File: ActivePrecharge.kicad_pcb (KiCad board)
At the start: 2 copper layers, 71.5 x 54.5 mm, 34 parts, among them Con1 LED, J1 Conn_01x03, J2 Conn_01x02, J3 Conn_01x02, Q1 IRLML0030, U1 NCP785AH50T1G, U2 NCP785AH50T1G, U3 TLV9301xDCK, U4 TCMT1106

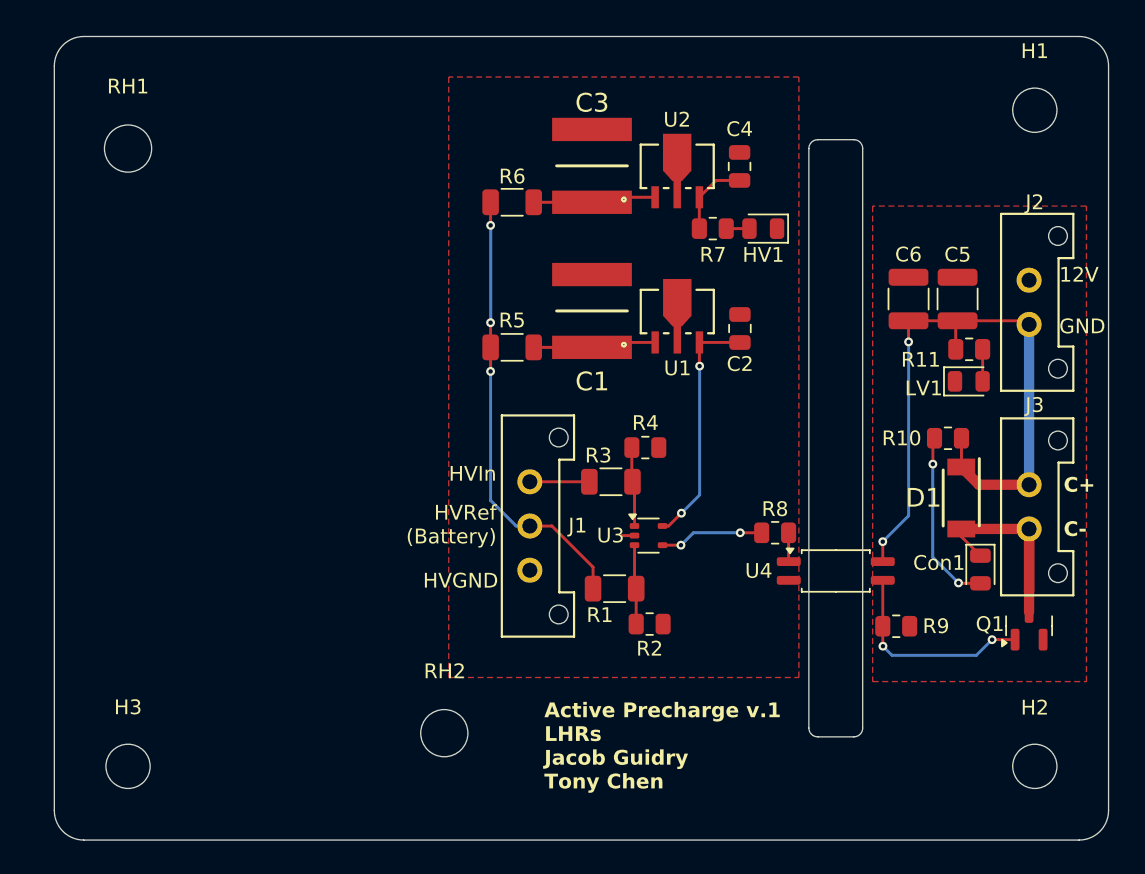
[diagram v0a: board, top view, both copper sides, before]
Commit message: 11/2 fixed incorrect footprint and symbol
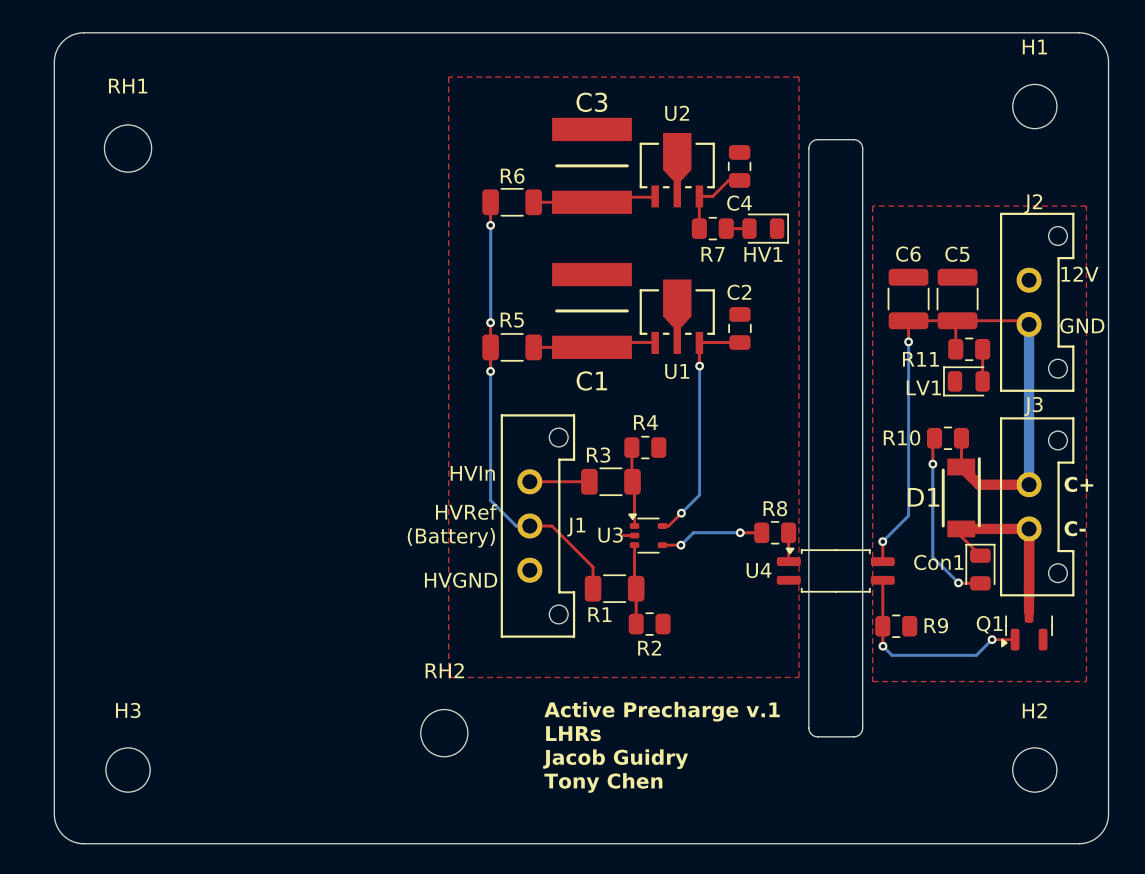
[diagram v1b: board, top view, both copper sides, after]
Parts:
- moved H1 0.25 mm to (140.8, 73.0)
- moved H2 0.25 mm to (140.8, 118.0)
- moved H3 0.25 mm to (79.2, 118.0)
- moved U2 0.06 mm to (116.5, 77.0)
- turned C2 to -90 degrees
- turned C4 to -90 degrees
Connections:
- C2 pad 1: /Vcc+ -> HVGND
- C2 pad 2: HVGND -> /Vcc+
- C4 pad 1: Net-(U2-OUT) -> HVGND
- C4 pad 2: HVGND -> Net-(U2-VOUT)
- R7 pad 1: Net-(U2-OUT) -> Net-(U2-VOUT)
- U2 pad 3: Net-(U2-OUT) -> Net-(U2-VOUT)
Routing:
- net Net-(U2-VOUT): track 0.00 -> 5.37 mm
- net Net-(U2-OUT): track 5.34 -> 0.00 mm
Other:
- board size 71.5 x 54.5 mm -> 71.5 x 55 mm

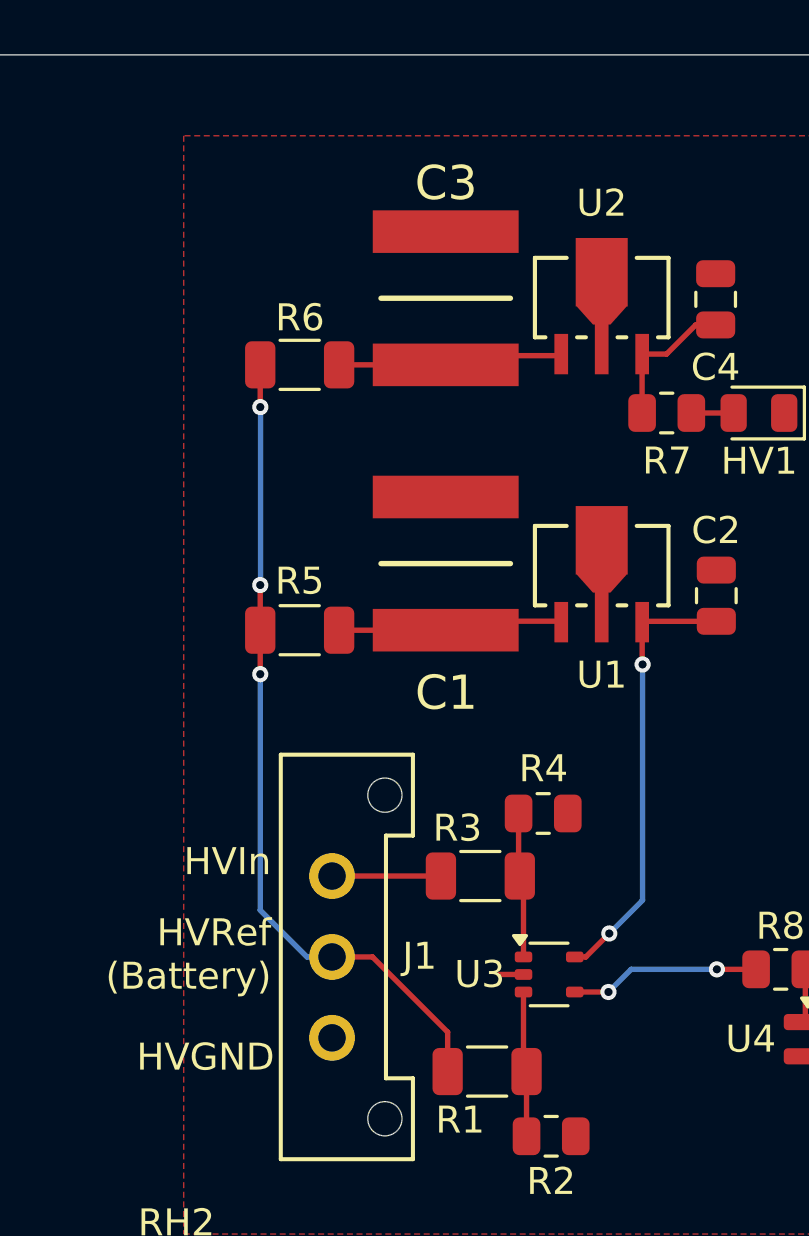
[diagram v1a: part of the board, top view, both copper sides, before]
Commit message: HV and trace routing fixes
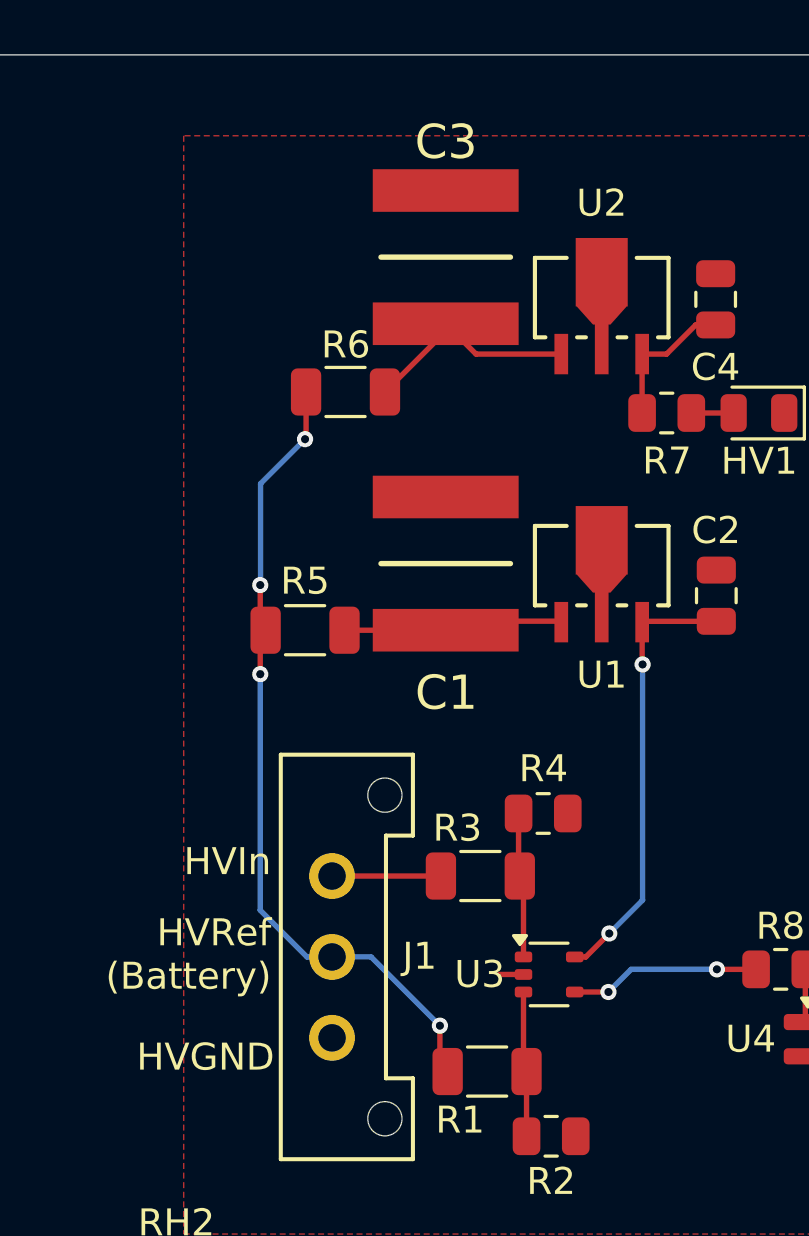
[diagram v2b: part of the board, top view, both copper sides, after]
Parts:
- moved R6 1.98 mm to (107.0, 80.5)
- moved C3 1.52 mm to (110.7, 75.5)
- moved R5 0.20 mm to (105.5, 89.3)
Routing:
- net HVRef: track 30.5 -> 30.2 mm, vias 3 -> 4
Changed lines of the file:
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@@
 	(footprint "Active-PrechargeLib:CAPC5750X220N"
 		(layer "F.Cu")
-		(at 110.7155 77.0245 90)
+		(at 110.7155 75.5 90)
 		(descr "2220-1")
 		(tags "Capacitor")
@@
 	(footprint "Resistor_SMD:R_1206_3216Metric"
 		(layer "F.Cu")
-		(at 105.3 89.3345)
+		(at 105.5 89.3345)
 		(descr "Resistor SMD 1206 (3216 Metric), square (rectangular) end terminal, IPC_7351 nominal, (Body size source: IPC-SM-782 page 72, https://www.pcb-3d.com/wordpress/wp-content/uploads/ipc-sm-782a_amendment_1_and_2.pdf), generated with kicad-footprint-generator")
 		(tags "resistor")
 		(property "Reference" "R5"
-			(at 0 -1.82 0)
+			(at 0 -1.82 360)
 			(layer "F.SilkS")
 			(effects
@@
 		)
 		(property "Value" "10k"
-			(at 0 1.82 0)
+			(at 0 1.82 360)
 			(layer "F.Fab")
 			(effects
@@
 		)
 		(fp_text user "${REFERENCE}"
-			(at 0 0 0)
+			(at 0 0 360)
 			(layer "F.Fab")
 			(effects
@@
 	(footprint "Resistor_SMD:R_1206_3216Metric"
 		(layer "F.Cu")
-		(at 105.3 79.4945 180)
+		(at 107 80.5 180)
 		(descr "Resistor SMD 1206 (3216 Metric), square (rectangular) end terminal, IPC_7351 nominal, (Body size source: IPC-SM-782 page 72, https://www.pcb-3d.com/wordpress/wp-content/uploads/ipc-sm-782a_amendment_1_and_2.pdf), generated with kicad-footprint-generator")
 		(tags "resistor")
@@
 	)
 	(segment
-		(start 103.8375 81.0575)
-		(end 103.8375 79.4945)
+		(start 110.5 104)
+		(end 110.5 105.4125)
 		(width 0.2)
 		(layer "F.Cu")
@@
 	)
 	(segment
-		(start 110.7875 104.2375)
-		(end 108 101.45)
+		(start 110.5 105.4125)
+		(end 110.7875 105.7)
 		(width 0.2)
 		(layer "F.Cu")
@@
 	)
 	(segment
-		(start 110.7875 105.7)
-		(end 110.7875 104.2375)
+		(start 105.5375 80.5)
+		(end 105.5375 82.2125)
 		(width 0.2)
 		(layer "F.Cu")
@@
 	)
 	(segment
-		(start 108 101.45)
-		(end 106.5 101.45)
-		(width 0.2)
-		(layer "F.Cu")
-		(net 7)
-	)
-	(segment
-		(start 103.84 81.06)
-		(end 103.8375 81.0575)
+		(start 105.5375 82.2125)
+		(end 105.5 82.25)
 		(width 0.2)
 		(layer "F.Cu")
@@
 	)
 	(via
-		(at 103.84 81.06)
+		(at 105.5 82.25)
 		(size 0.6)
 		(drill 0.3)
@@
 		(net 7)
 	)
+	(via
+		(at 110.5 104)
+		(size 0.6)
+		(drill 0.3)
+		(layers "F.Cu" "B.Cu")
+		(net 7)
+	)
 	(segment
-		(start 103.85 87.6475)
-		(end 103.85 81.07)
+		(start 105.57 101.45)
+		(end 103.8375 99.7175)
 		(width 0.2)
 		(layer "B.Cu")
@@
 	)
 	(segment
-		(start 105.57 101.45)
-		(end 103.8375 99.7175)
+		(start 103.85 87.6475)
+		(end 103.8375 87.66)
 		(width 0.2)
 		(layer "B.Cu")
@@
 	)
 	(segment
-		(start 103.85 81.07)
-		(end 103.84 81.06)
+		(start 106.5 101.45)
+		(end 107.95 101.45)
 		(width 0.2)
 		(layer "B.Cu")
@@
 	)
 	(segment
-		(start 103.8375 87.66)
+		(start 105.5 82.25)
+		(end 103.85 83.9)
+		(width 0.2)
+		(layer "B.Cu")
+		(net 7)
+	)
+	(segment
+		(start 103.85 83.9)
 		(end 103.85 87.6475)
 		(width 0.2)
@@
 	)
 	(segment
+		(start 107.95 101.45)
+		(end 110.5 104)
+		(width 0.2)
+		(layer "B.Cu")
+		(net 7)
+	)
+	(segment
 		(start 106.5 101.45)
 		(end 105.57 101.45)
@@
 	)
 	(segment
-		(start 110.7155 79.4945)
-		(end 106.7625 79.4945)
+		(start 115 79.0955)
+		(end 111.841 79.0955)
+		(width 0.2)
+		(layer "F.Cu")
+		(net 17)
+	)
+	(segment
+		(start 111.841 79.0955)
+		(end 110.7155 77.97)
 		(width 0.2)
 		(layer "F.Cu")
@@
 	)
 	(segment
-		(start 114.9955 79.1535)
-		(end 111.0565 79.1535)
+		(start 108.4625 80.5)
+		(end 110.7155 78.247)
 		(width 0.2)
 		(layer "F.Cu")
@@
 	)
 	(segment
-		(start 111.0565 79.1535)
-		(end 110.7155 79.4945)
+		(start 110.7155 78.247)
+		(end 110.7155 77.97)
 		(width 0.2)
 		(layer "F.Cu")

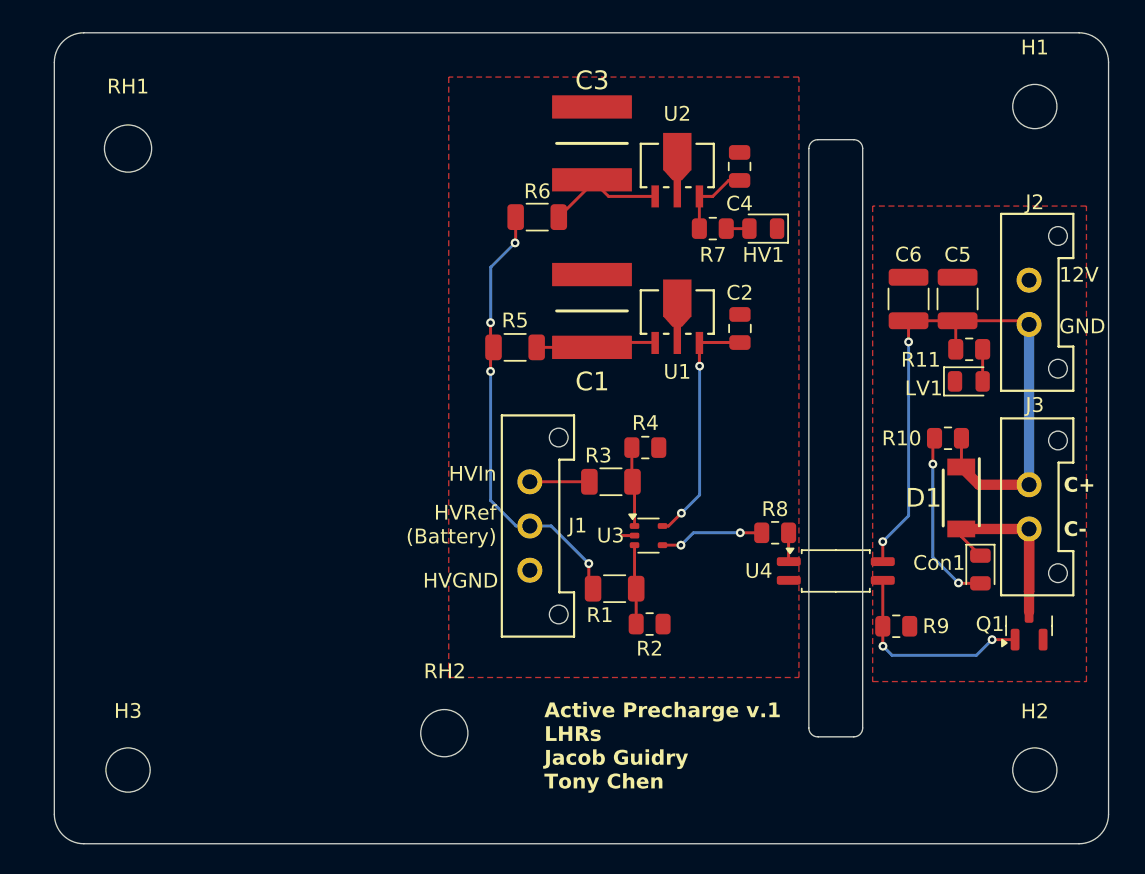
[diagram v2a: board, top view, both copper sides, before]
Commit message: dimension checks and silkscreen additions
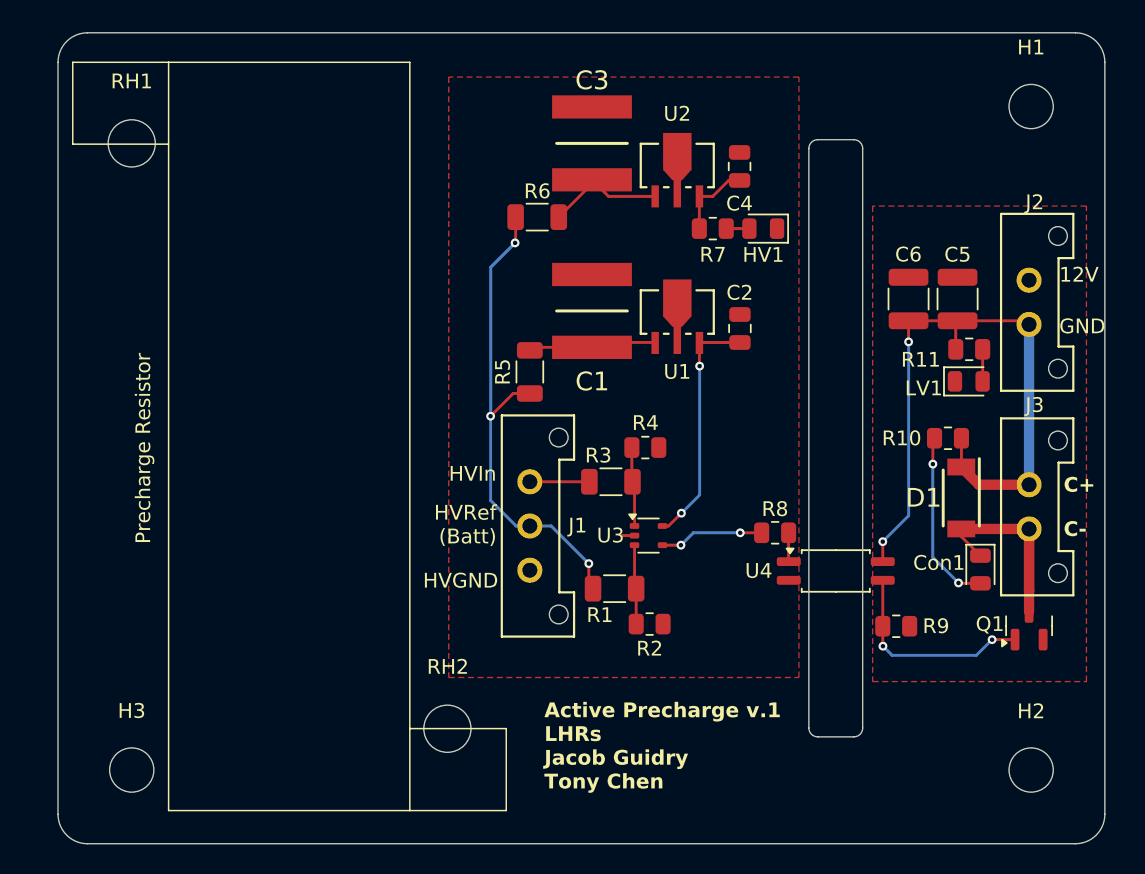
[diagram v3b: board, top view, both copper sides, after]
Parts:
- moved R5 1.94 mm to (106.5, 91.0), turned to 90 degrees
- moved RH1 0.43 mm to (79.5, 75.5)
- moved RH2 0.37 mm to (100.9, 115.2)
- moved H1 0.25 mm to (140.5, 73.0)
- moved H2 0.25 mm to (140.5, 118.0)
- moved H3 0.25 mm to (79.5, 118.0)
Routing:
- net HVRef: track 30.2 -> 33.5 mm, vias 4 -> 3
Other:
- board size 71.5 x 55 mm -> 71 x 55 mm
- board text added: "HVRef (Batt)"
- board text added: "Hypotenuse should be ~45.09 for legs 39.67 and 21.44"
- board text removed: "HVRef (Battery)"
